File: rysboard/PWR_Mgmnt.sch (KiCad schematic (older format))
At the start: 14 parts

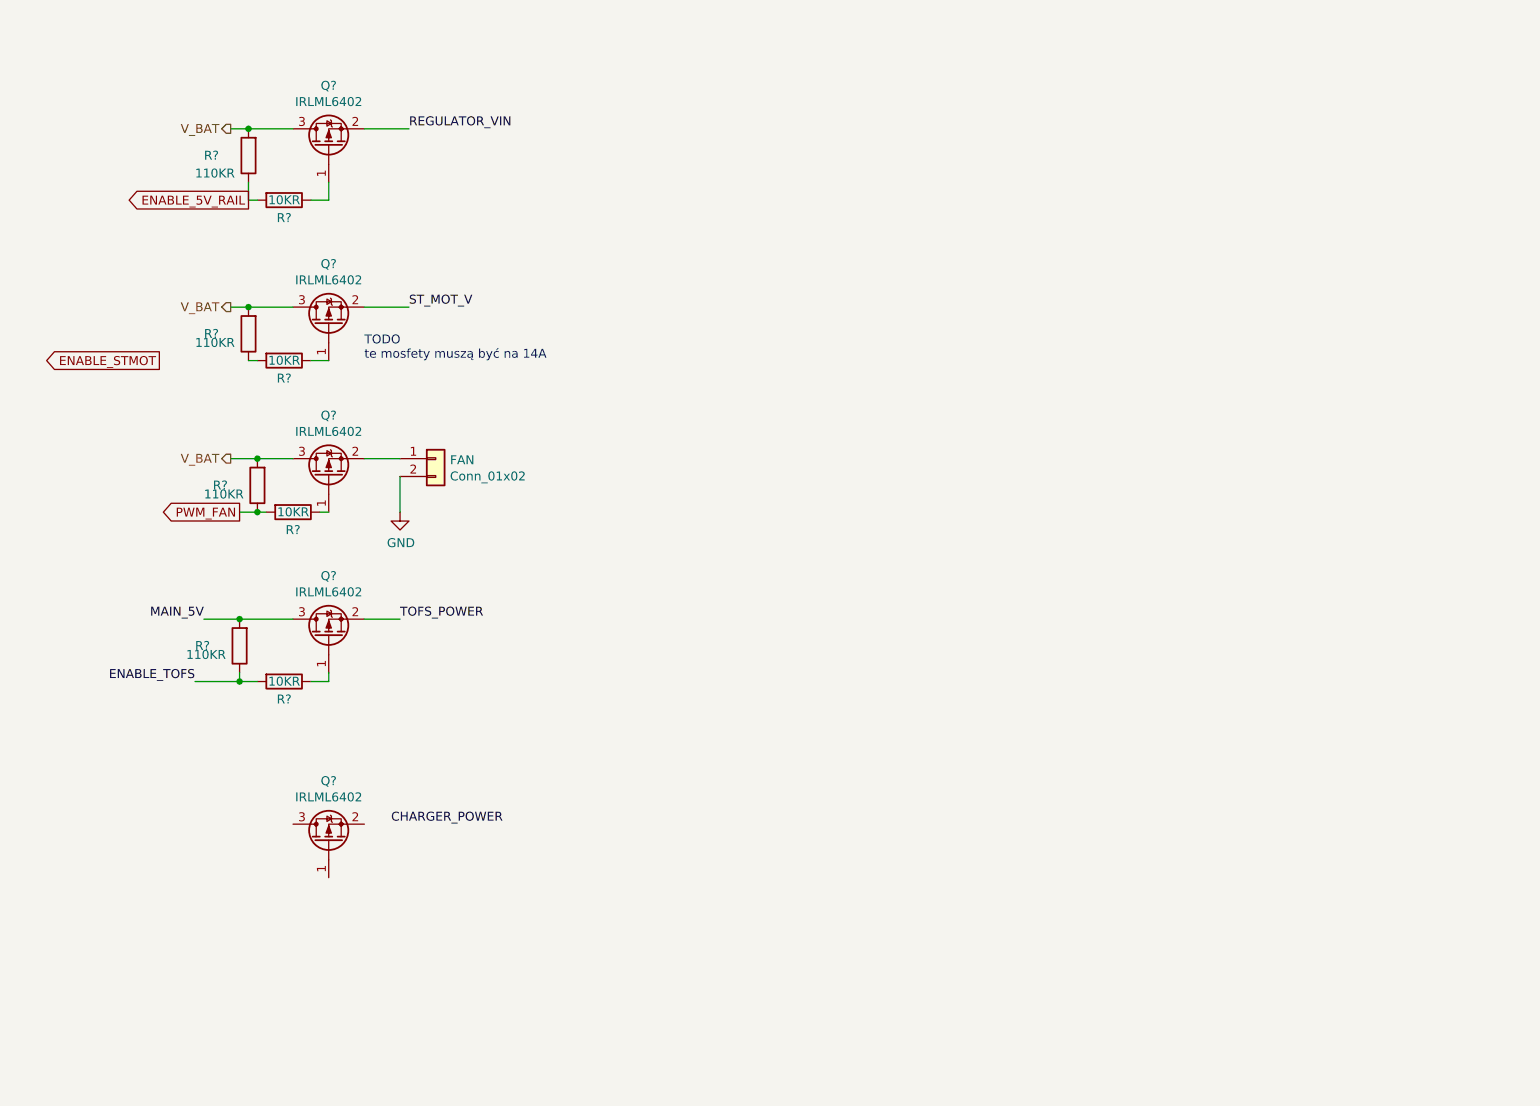
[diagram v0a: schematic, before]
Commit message: Added mcu, labeled its pins , major powwer supply overhaul started
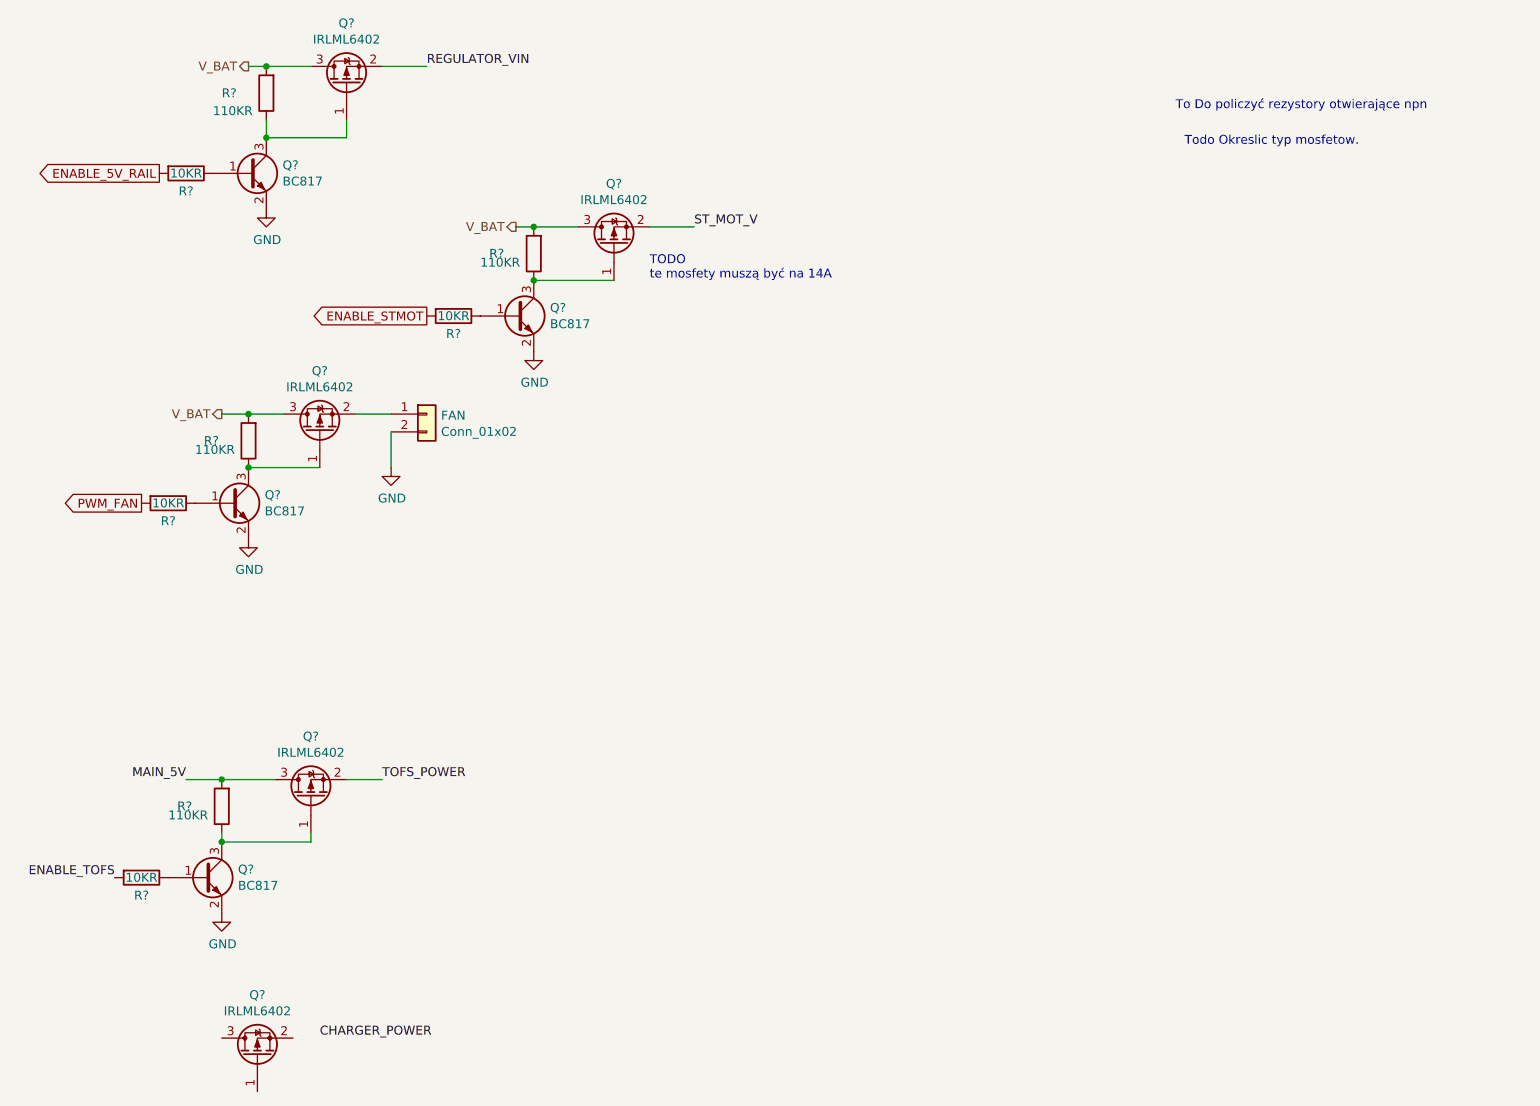
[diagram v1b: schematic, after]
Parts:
- added Q? (x4): BC817, Package_TO_SOT_SMD:SOT-23, symbol Transistor_BJT:BC817
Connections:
- net ENABLE_5V_RAIL: no longer R?.1
- net ENABLE_STMOT: now also R?.2
- net ENABLE_TOFS: no longer R?.1
- net GND: now also Q?.2 (E), Q?.2 (E), Q?.2 (E), Q?.2 (E)
- net PWM_FAN: no longer R?.1
- net at Q?.1 (G): now also R?.1, Q?.3 (C); no longer R?.1 (x4)
- new net: Q?.1 (B), R?.1 (x4)
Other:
- note added: "To Do policzyć rezystory otwierające npn"
- note added: "Todo Okreslic typ mosfetow.\n"
- moved on the sheet: FAN, Q?, R?

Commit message: DMP3036SSD footprint added
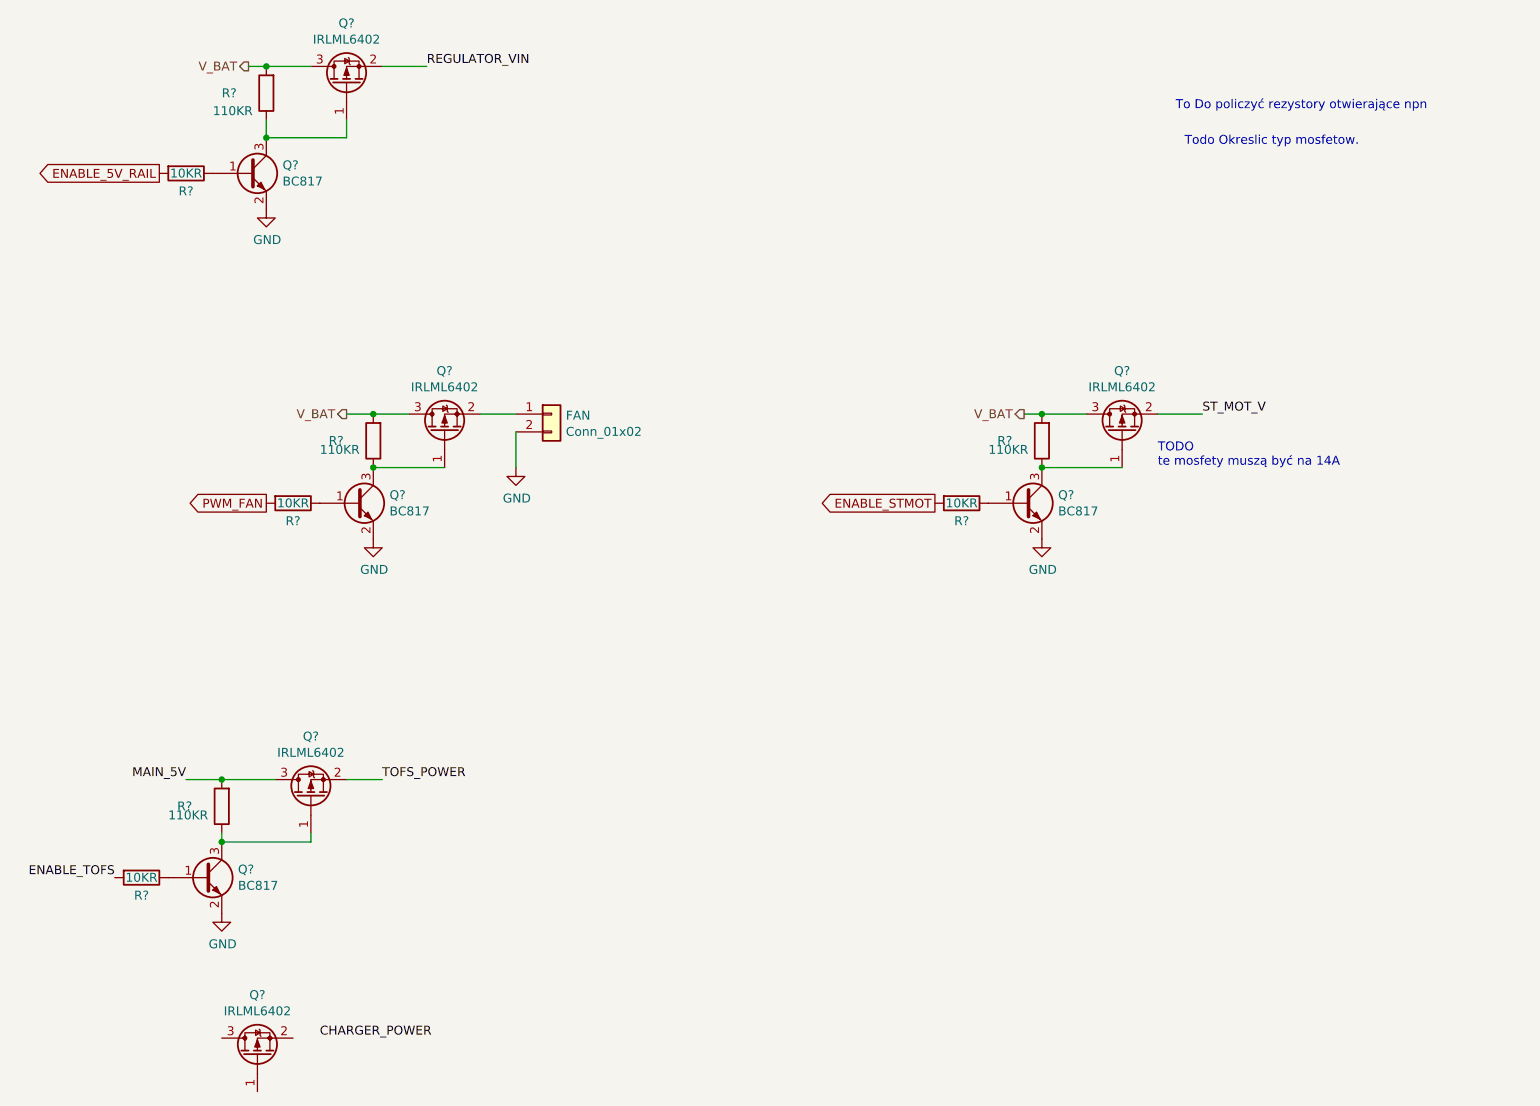
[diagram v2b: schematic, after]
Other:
- moved on the sheet: FAN, Q?, R?
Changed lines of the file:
@@
 L Transistor_FET:IRLML6402 Q?
 U 1 1 5FF1B166
-P 3850 2050
-F 0 "Q?" V 4192 2050 50  0000 C CNN
-F 1 "IRLML6402" V 4101 2050 50  0000 C CNN
-F 2 "Package_TO_SOT_SMD:SOT-23" H 4050 1975 50  0001 L CIN
-F 3 "https://www.infineon.com/dgdl/irlml6402pbf.pdf?fileId=5546d462533600a401535668d5c2263c" H 3850 2050 50  0001 L CNN
-	1    3850 2050
+P 6700 3100
+F 0 "Q?" V 7042 3100 50  0000 C CNN
+F 1 "IRLML6402" V 6951 3100 50  0000 C CNN
+F 2 "Package_TO_SOT_SMD:SOT-23" H 6900 3025 50  0001 L CIN
+F 3 "https://www.infineon.com/dgdl/irlml6402pbf.pdf?fileId=5546d462533600a401535668d5c2263c" H 6700 3100 50  0001 L CNN
+	1    6700 3100
 	0    -1   -1   0
 $EndComp
@@
 L Device:R R?
 U 1 1 5FF1B724
-P 2950 2450
-F 0 "R?" V 3050 2450 50  0000 C CNN
-F 1 "10KR" V 2950 2450 50  0000 C CNN
-F 2 "" V 2880 2450 50  0001 C CNN
-F 3 "~" H 2950 2450 50  0001 C CNN
-	1    2950 2450
+P 5800 3500
+F 0 "R?" V 5900 3500 50  0000 C CNN
+F 1 "10KR" V 5800 3500 50  0000 C CNN
+F 2 "" V 5730 3500 50  0001 C CNN
+F 3 "~" H 5800 3500 50  0001 C CNN
+	1    5800 3500
 	0    1    1    0
 $EndComp
@@
 L Device:R R?
 U 1 1 5FF1BA45
-P 3400 2100
-F 0 "R?" H 3650 2100 50  0000 R CNN
-F 1 "110KR" H 3700 2150 50  0000 R CNN
-F 2 "" V 3330 2100 50  0001 C CNN
-F 3 "~" H 3400 2100 50  0001 C CNN
-	1    3400 2100
+P 6250 3150
+F 0 "R?" H 6500 3150 50  0000 R CNN
+F 1 "110KR" H 6550 3200 50  0000 R CNN
+F 2 "" V 6180 3150 50  0001 C CNN
+F 3 "~" H 6250 3150 50  0001 C CNN
+	1    6250 3150
 	-1   0    0    1
 $EndComp
 Wire Wire Line
-	3300 1950 3400 1950
-Connection ~ 3400 1950
-Wire Wire Line
-	3400 1950 3650 1950
-Text GLabel 2800 2450 0    50   Output ~ 0
+	6150 3000 6250 3000
+Connection ~ 6250 3000
+Wire Wire Line
+	6250 3000 6500 3000
+Text GLabel 5650 3500 0    50   Output ~ 0
 ENABLE_STMOT
 $Comp
 L Transistor_FET:IRLML6402 Q?
 U 1 1 5FF1C5A5
-P 2200 3100
-F 0 "Q?" V 2542 3100 50  0000 C CNN
-F 1 "IRLML6402" V 2451 3100 50  0000 C CNN
-F 2 "Package_TO_SOT_SMD:SOT-23" H 2400 3025 50  0001 L CIN
-F 3 "https://www.infineon.com/dgdl/irlml6402pbf.pdf?fileId=5546d462533600a401535668d5c2263c" H 2200 3100 50  0001 L CNN
-	1    2200 3100
+P 2900 3100
+F 0 "Q?" V 3242 3100 50  0000 C CNN
+F 1 "IRLML6402" V 3151 3100 50  0000 C CNN
+F 2 "Package_TO_SOT_SMD:SOT-23" H 3100 3025 50  0001 L CIN
+F 3 "https://www.infineon.com/dgdl/irlml6402pbf.pdf?fileId=5546d462533600a401535668d5c2263c" H 2900 3100 50  0001 L CNN
+	1    2900 3100
 	0    -1   -1   0
 $EndComp
@@
 L Device:R R?
 U 1 1 5FF1D639
-P 1350 3500
-F 0 "R?" V 1450 3500 50  0000 C CNN
-F 1 "10KR" V 1350 3500 50  0000 C CNN
-F 2 "" V 1280 3500 50  0001 C CNN
-F 3 "~" H 1350 3500 50  0001 C CNN
-	1    1350 3500
+P 2050 3500
+F 0 "R?" V 2150 3500 50  0000 C CNN
+F 1 "10KR" V 2050 3500 50  0000 C CNN
+F 2 "" V 1980 3500 50  0001 C CNN
+F 3 "~" H 2050 3500 50  0001 C CNN
+	1    2050 3500
 	0    1    1    0
 $EndComp
-Text GLabel 1200 3500 0    50   Output ~ 0
+Text GLabel 1900 3500 0    50   Output ~ 0
 PWM_FAN
 $Comp
 L Device:R R?
 U 1 1 5FF1DBBE
-P 1800 3150
-F 0 "R?" H 2050 3150 50  0000 R CNN
-F 1 "110KR" H 2100 3200 50  0000 R CNN
-F 2 "" V 1730 3150 50  0001 C CNN
-F 3 "~" H 1800 3150 50  0001 C CNN
-	1    1800 3150
+P 2500 3150
+F 0 "R?" H 2750 3150 50  0000 R CNN
+F 1 "110KR" H 2800 3200 50  0000 R CNN
+F 2 "" V 2430 3150 50  0001 C CNN
+F 3 "~" H 2500 3150 50  0001 C CNN
+	1    2500 3150
 	-1   0    0    1
 $EndComp
 Wire Wire Line
-	1650 3000 1800 3000
-Connection ~ 1800 3000
-Wire Wire Line
-	1800 3000 2000 3000
-Connection ~ 1800 3300
+	2350 3000 2500 3000
+Connection ~ 2500 3000
+Wire Wire Line
+	2500 3000 2700 3000
+Connection ~ 2500 3300
 $Comp
 L Connector_Generic:Conn_01x02 FAN
 U 1 1 5FF2B8C7
-P 2800 3000
-F 0 "FAN" H 2880 2992 50  0000 L CNN
-F 1 "Conn_01x02" H 2880 2901 50  0000 L CNN
-F 2 "Connector_PinHeader_2.54mm:PinHeader_1x02_P2.54mm_Vertical" H 2800 3000 50  0001 C CNN
-F 3 "~" H 2800 3000 50  0001 C CNN
-	1    2800 3000
-	1    0    0    -1
-$EndComp
-Wire Wire Line
-	2600 3000 2400 3000
+P 3500 3000
+F 0 "FAN" H 3580 2992 50  0000 L CNN
+F 1 "Conn_01x02" H 3580 2901 50  0000 L CNN
+F 2 "Connector_PinHeader_2.54mm:PinHeader_1x02_P2.54mm_Vertical" H 3500 3000 50  0001 C CNN
+F 3 "~" H 3500 3000 50  0001 C CNN
+	1    3500 3000
+	1    0    0    -1
+$EndComp
+Wire Wire Line
+	3300 3000 3100 3000
 $Comp
 L power:GND #PWR?
 U 1 1 5FF2C212
-P 2600 3300
-F 0 "#PWR?" H 2600 3050 50  0001 C CNN
-F 1 "GND" H 2605 3127 50  0000 C CNN
-F 2 "" H 2600 3300 50  0001 C CNN
-F 3 "" H 2600 3300 50  0001 C CNN
-	1    2600 3300
-	1    0    0    -1
-$EndComp
-Wire Wire Line
-	2600 3300 2600 3100
+P 3300 3300
+F 0 "#PWR?" H 3300 3050 50  0001 C CNN
+F 1 "GND" H 3305 3127 50  0000 C CNN
+F 2 "" H 3300 3300 50  0001 C CNN
+F 3 "" H 3300 3300 50  0001 C CNN
+	1    3300 3300
+	1    0    0    -1
+$EndComp
+Wire Wire Line
+	3300 3300 3300 3100
 $Comp
 L Device:R R?
@@
 Wire Wire Line
 	1450 5050 1650 5050
-Text Notes 4050 2250 0    50   ~ 0
+Text Notes 6900 3300 0    50   ~ 0
 TODO\nte mosfety muszą być na 14A
-Text Label 4300 1950 0    50   ~ 0
+Text Label 7150 3000 0    50   ~ 0
 ST_MOT_V
 Wire Wire Line
-	4300 1950 4050 1950
+	7150 3000 6900 3000
 Text Label 2800 1050 0    50   ~ 0
 REGULATOR_VIN
@@
 Text HLabel 1800 1050 0    50   Output ~ 0
 V_BAT
-Text HLabel 3300 1950 0    50   Output ~ 0
+Text HLabel 6150 3000 0    50   Output ~ 0
 V_BAT
-Text HLabel 1650 3000 0    50   Output ~ 0
+Text HLabel 2350 3000 0    50   Output ~ 0
 V_BAT
 Text Label 2200 6500 0    50   ~ 0
@@
 	1    0    0    -1
 $EndComp
-Connection ~ 3400 2250
-Wire Wire Line
-	3400 2250 3850 2250
+Connection ~ 6250 3300
+Wire Wire Line
+	6250 3300 6700 3300
 $Comp
 L power:GND #PWR?
 U 1 1 60326820
-P 3400 2650
-F 0 "#PWR?" H 3400 2400 50  0001 C CNN
-F 1 "GND" H 3405 2477 50  0000 C CNN
-F 2 "" H 3400 2650 50  0001 C CNN
-F 3 "" H 3400 2650 50  0001 C CNN
-	1    3400 2650
+P 6250 3700
+F 0 "#PWR?" H 6250 3450 50  0001 C CNN
+F 1 "GND" H 6255 3527 50  0000 C CNN
+F 2 "" H 6250 3700 50  0001 C CNN
+F 3 "" H 6250 3700 50  0001 C CNN
+	1    6250 3700
 	1    0    0    -1
 $EndComp
@@
 L Transistor_BJT:BC817 Q?
 U 1 1 60329A38
-P 3300 2450
-F 0 "Q?" H 3491 2496 50  0000 L CNN
-F 1 "BC817" H 3491 2405 50  0000 L CNN
-F 2 "Package_TO_SOT_SMD:SOT-23" H 3500 2375 50  0001 L CIN
-F 3 "http://www.fairchildsemi.com/ds/BC/BC817.pdf" H 3300 2450 50  0001 L CNN
-	1    3300 2450
+P 6150 3500
+F 0 "Q?" H 6341 3546 50  0000 L CNN
+F 1 "BC817" H 6341 3455 50  0000 L CNN
+F 2 "Package_TO_SOT_SMD:SOT-23" H 6350 3425 50  0001 L CIN
+F 3 "http://www.fairchildsemi.com/ds/BC/BC817.pdf" H 6150 3500 50  0001 L CNN
+	1    6150 3500
 	1    0    0    -1
 $EndComp
@@
 L Transistor_BJT:BC817 Q?
 U 1 1 6032D6E0
-P 1700 3500
-F 0 "Q?" H 1891 3546 50  0000 L CNN
-F 1 "BC817" H 1891 3455 50  0000 L CNN
-F 2 "Package_TO_SOT_SMD:SOT-23" H 1900 3425 50  0001 L CIN
-F 3 "http://www.fairchildsemi.com/ds/BC/BC817.pdf" H 1700 3500 50  0001 L CNN
-	1    1700 3500
-	1    0    0    -1
-$EndComp
-Wire Wire Line
-	1800 3300 2200 3300
+P 2400 3500
+F 0 "Q?" H 2591 3546 50  0000 L CNN
+F 1 "BC817" H 2591 3455 50  0000 L CNN
+F 2 "Package_TO_SOT_SMD:SOT-23" H 2600 3425 50  0001 L CIN
+F 3 "http://www.fairchildsemi.com/ds/BC/BC817.pdf" H 2400 3500 50  0001 L CNN
+	1    2400 3500
+	1    0    0    -1
+$EndComp
+Wire Wire Line
+	2500 3300 2900 3300
 $Comp
 L power:GND #PWR?
 U 1 1 60330124
-P 1800 3700
-F 0 "#PWR?" H 1800 3450 50  0001 C CNN
-F 1 "GND" H 1805 3527 50  0000 C CNN
-F 2 "" H 1800 3700 50  0001 C CNN
-F 3 "" H 1800 3700 50  0001 C CNN
-	1    1800 3700
-	1    0    0    -1
-$EndComp
+P 2500 3700
+F 0 "#PWR?" H 2500 3450 50  0001 C CNN
+F 1 "GND" H 2505 3527 50  0000 C CNN
+F 2 "" H 2500 3700 50  0001 C CNN
+F 3 "" H 2500 3700 50  0001 C CNN
+	1    2500 3700
+	1    0    0    -1
+$EndComp

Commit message: NST847BDP6T5G Added, more conections done
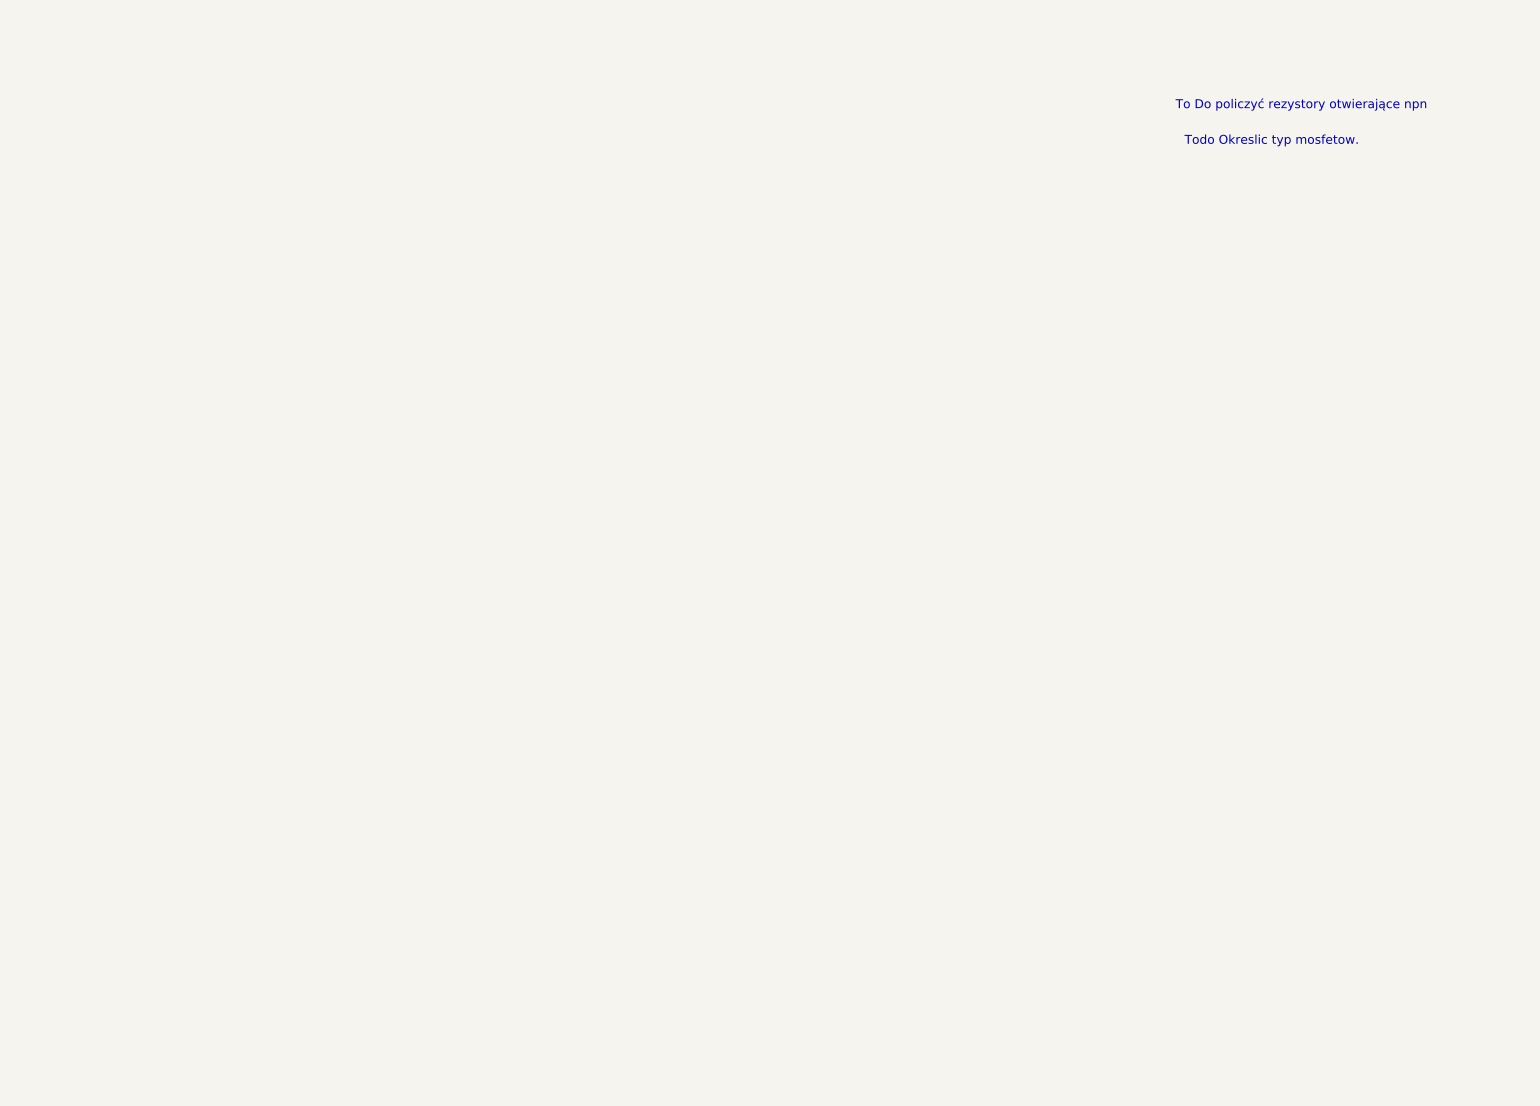
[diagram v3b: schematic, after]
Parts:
- removed FAN: Conn_01x02, Connector_PinHeader_2.54mm:PinHeader_1x02_P2.54mm_Vertical, symbol Connector_Generic:Conn_01x02
- removed Q? (x5): IRLML6402, Package_TO_SOT_SMD:SOT-23, symbol Transistor_FET:IRLML6402
- removed Q? (x4): BC817, Package_TO_SOT_SMD:SOT-23, symbol Transistor_BJT:BC817
- removed R? (x4): 10KR, symbol Device:R
- removed R? (x4): 110KR, symbol Device:R
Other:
- note removed: "TODO\nte mosfety muszą być na 14A"
